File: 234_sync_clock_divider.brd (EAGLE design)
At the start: 93 x 19 mm, 25 parts, among them IC1 4022N, IC2 78L05Z, Q1 BC547B

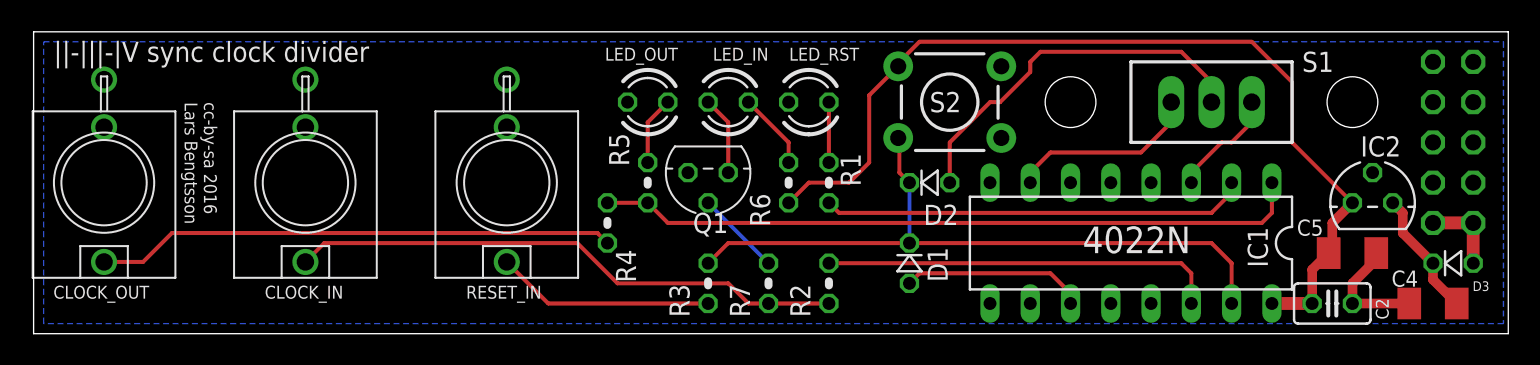
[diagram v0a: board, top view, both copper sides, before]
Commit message: Moved power connector - it was a bit too close to board edge. Added notice about CC license.
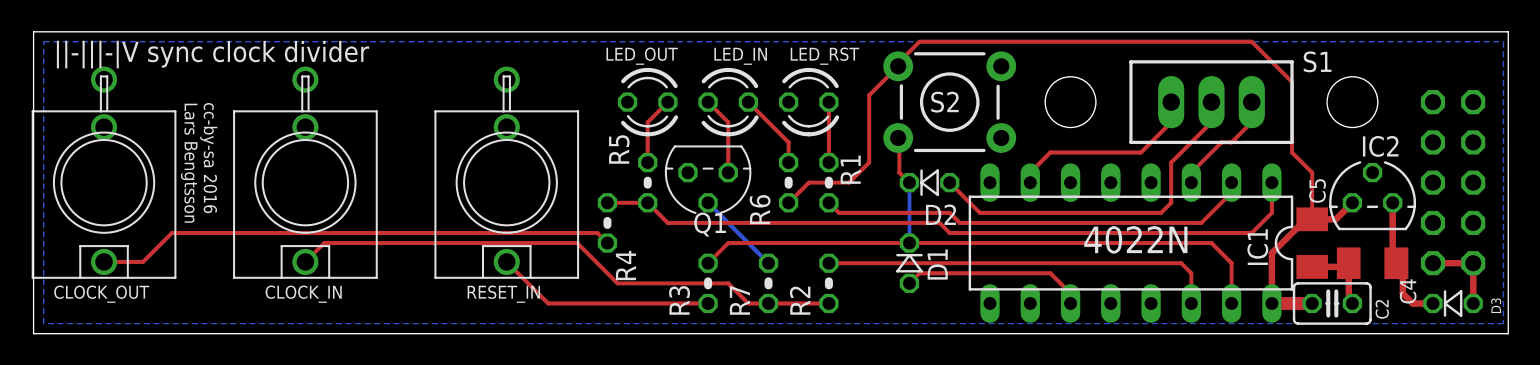
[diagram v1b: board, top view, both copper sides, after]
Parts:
- moved C4 4.58 mm to (87.6, 25.4)
- moved C5 2.62 mm to (83.8, 26.7), turned to 270 degrees
- moved JP1 2.54 mm to (92.7, 30.5)
- moved D3 2.54 mm to (92.7, 22.9)
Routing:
- net GND: track 7.38 -> 5.04 mm
- net +5V: track 58.8 -> 61.0 mm
- net N$13: track 23.8 -> 22.4 mm
- net N$7: track 44.6 -> 45.1 mm
- net N$4: track 26.8 -> 27.4 mm
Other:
- board text added: "*** RED STRIPE/-12V"
- board text added: "2/3/4 sync clock divider cc by-sa 2016 Lars Bengtsson"
- board text removed: "2/3/4 sync clock divider"
- board text removed: "<- RED STRIPE/-12V"
